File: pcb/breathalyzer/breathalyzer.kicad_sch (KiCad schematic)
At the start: 8 parts, among them U1 STM32F030K6Tx, U2 TLV73325PDBV

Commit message: voltage reference
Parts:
- added IC1: TPS3840DL25DBVR, SOT95P280X145-5N, symbol breathalyzer:TPS3840DL25DBVR
- added R1: 100k, Resistor_SMD:R_0402_1005Metric, symbol Device:R
- C1: footprint (none) -> Capacitor_SMD:C_01005_0402Metric
- C2, C3: footprint (none) -> Capacitor_SMD:C_0402_1005Metric
- C4, C5: value 100 nf -> 1 uF; footprint (none) -> Capacitor_SMD:C_0603_1608Metric
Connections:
- net +BATT: now also IC1.2 (VDD), R1.1; no longer U2.3 (EN)
- net GND: now also IC1.3 (GND)
- new net: IC1.1 (~{RESET}), R1.2, U2.3 (EN)
- no-connect marks 0 -> 2
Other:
- moved on the sheet: C4, U2

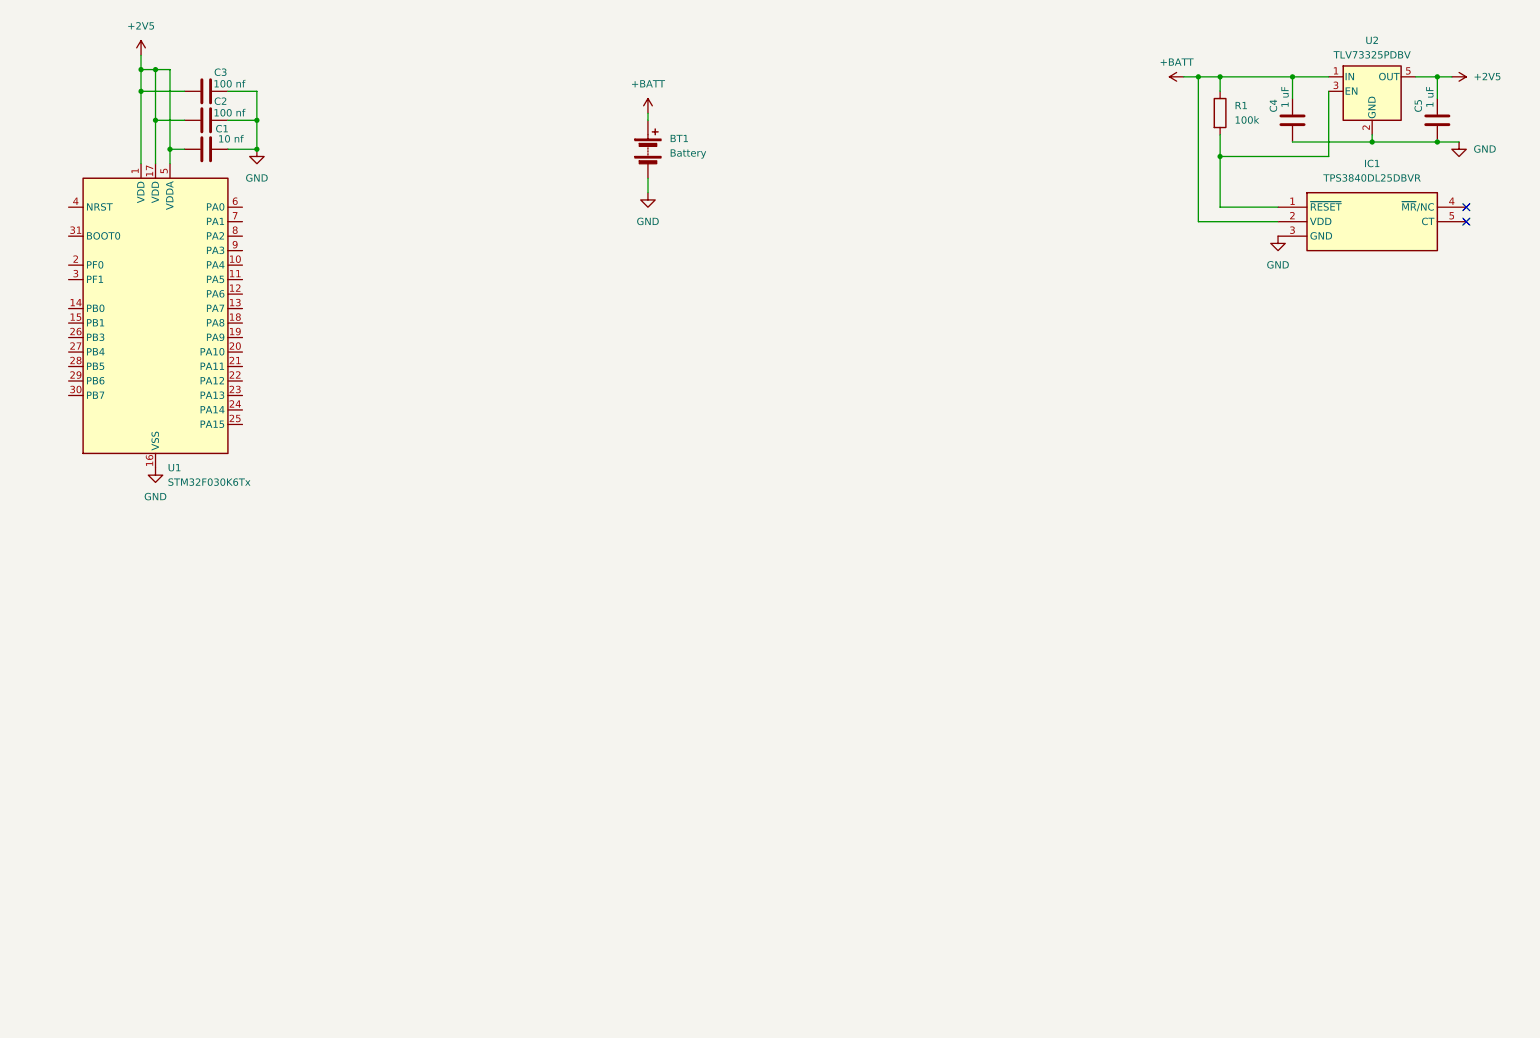
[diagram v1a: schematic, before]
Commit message: boost 3v3
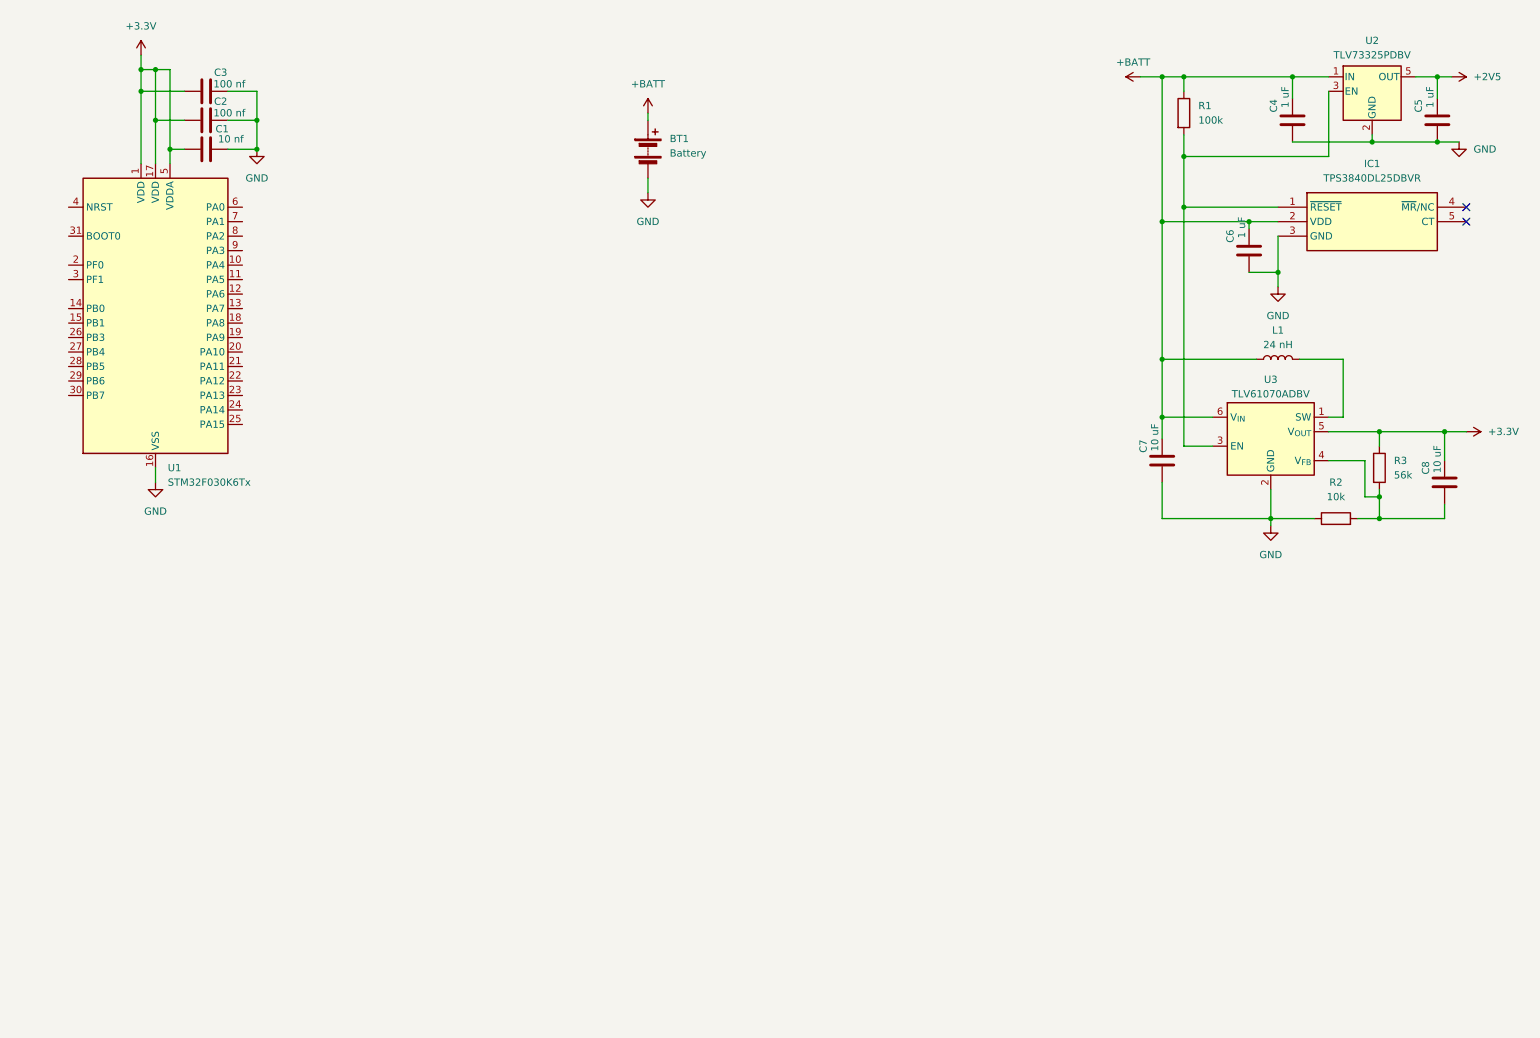
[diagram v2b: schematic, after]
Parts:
- added C6: 1 uF, Capacitor_SMD:C_0603_1608Metric, symbol Device:C
- added C7, C8: 10 uF, Capacitor_SMD:C_0805_2012Metric, symbol Device:C
- added L1: 24 nH, Inductor_SMD:L_1008_2520Metric, symbol Device:L
- added R2: 10k, Resistor_SMD:R_0603_1608Metric, symbol Device:R
- added R3: 56k, Resistor_SMD:R_0603_1608Metric, symbol Device:R
- added U3: TLV61070ADBV, Package_TO_SOT_SMD:SOT-23-6, symbol Regulator_Switching:TLV61070ADBV
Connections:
- net +2V5: no longer C1.1, C2.1, C3.1, U1.1 (VDD), U1.17 (VDD), U1.5 (VDDA)
- net +BATT: now also C6.2, C7.2, L1.1, U3.6 (V_{IN})
- net GND: now also C6.1, C7.1, R2.1, U3.2 (GND)
- net at IC1.1 (~{RESET}), R1.2, U2.3 (EN): now also U3.3 (EN)
- new net: L1.2, U3.1 (SW)
- new net: C8.1, R2.2, R3.2, U3.4 (V_{FB})
- new net +3.3V: C1.1, C2.1, C3.1, C8.2, R3.1, U1.1 (VDD), U1.17 (VDD), U1.5 (VDDA), U3.5 (V_{OUT})
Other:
- moved on the sheet: R1

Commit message: program MCU
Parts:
- added J1: 10129379-906002BLF, HDRRA6W67P0X254_1X6_1524X254X241P, symbol breathalyzer:10129379-906002BLF
- added R4: 4k7, Resistor_SMD:R_1206_3216Metric, symbol Device:R
- IC1: footprint SOT95P280X145-5N -> Package_TO_SOT_SMD:SOT-23-5_HandSoldering
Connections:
- net GND: now also J1.1, R4.2
- net USART1_TX: now reaches U1.19 (PA9)
- net USART1_TX: now also J1.3
- net USART1_RX: now reaches U1.20 (PA10)
- net USART1_RX: now also J1.2
- net BOOT0: now reaches U1.31 (BOOT0)
- net BOOT0: now also J1.4, R4.1
- net +3.3V renamed +3V3

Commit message: Serial debug
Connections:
- net SWCLK: now reaches J1.5
- net SWCLK: now also U1.24 (PA14)
- net SWDIO: now reaches J1.6
- net SWDIO: now also U1.23 (PA13)
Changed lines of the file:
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@@
+		)
+	)
+	(global_label "SWDIO"
+		(shape input)
+		(at 59.69 80.01 0)
+		(fields_autoplaced yes)
+		(effects
+			(font
+				(size 1.27 1.27)
+			)
+			(justify left)
+		)
+		(property "Intersheetrefs" "${INTERSHEET_REFS}"
+			(at 68.5414 80.01 0)
+			(effects
+				(font
+					(size 1.27 1.27)
+				)
+				(justify left)
+				(hide yes)
+			)
 		)
 	)
@@
 				)
 				(justify left)
+				(hide yes)
+			)
+		)
+	)
+	(global_label "SWCLK"
+		(shape input)
+		(at 59.69 82.55 0)
+		(fields_autoplaced yes)
+		(effects
+			(font
+				(size 1.27 1.27)
+			)
+			(justify left)
+		)
+		(property "Intersheetrefs" "${INTERSHEET_REFS}"
+			(at 68.9042 82.55 0)
+			(effects
+				(font
+					(size 1.27 1.27)
+				)
+				(justify left)
+				(hide yes)
+			)
+		)
+	)
+	(global_label "SWDIO"
+		(shape input)
+		(at 48.26 181.61 180)
+		(fields_autoplaced yes)
+		(effects
+			(font
+				(size 1.27 1.27)
+			)
+			(justify right)
+		)
+		(property "Intersheetrefs" "${INTERSHEET_REFS}"
+			(at 39.4086 181.61 0)
+			(effects
+				(font
+					(size 1.27 1.27)
+				)
+				(justify right)
 				(hide yes)
 			)
@@
 				(hide yes)
 			)
+		)
+	)
+	(global_label "SWCLK"
+		(shape input)
+		(at 48.26 179.07 180)
+		(fields_autoplaced yes)
+		(effects
+			(font
+				(size 1.27 1.27)
+			)
+			(justify right)
+		)
+		(property "Intersheetrefs" "${INTERSHEET_REFS}"
+			(at 39.0458 179.07 0)
+			(effects
+				(font
+					(size 1.27 1.27)
+				)
+				(justify right)
+				(hide yes)
+			)

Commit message: reset button
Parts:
- added SW1: PTS636SK43SMTR, breathalyzer:PTS636SM43JSMTRLFS, symbol Switch:SW_Push
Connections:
- net GND: now also SW1.2
- net NRST: now reaches U1.4 (NRST)
- net NRST: now also SW1.1
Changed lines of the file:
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@@
+	(wire
+		(pts
+			(xy 35.56 133.35) (xy 38.1 133.35)
+		)
+		(stroke
+			(width 0)
+			(type default)
+		)
+	)
 	(wire
 		(pts
@@
 		(pts
 			(xy 224.79 38.1) (xy 250.19 38.1)
+		)
+		(stroke
+			(width 0)
+			(type default)
+		)
+	)
+	(wire
+		(pts
+			(xy 48.26 133.35) (xy 50.8 133.35)
 		)
 		(stroke
@@
 		)
 	)
+	(global_label "NRST"
+		(shape input)
+		(at 29.21 46.99 180)
+		(fields_autoplaced yes)
+		(effects
+			(font
+				(size 1.27 1.27)
+			)
+			(justify right)
+		)
+		(property "Intersheetrefs" "${INTERSHEET_REFS}"
+			(at 21.4472 46.99 0)
+			(effects
+				(font
+					(size 1.27 1.27)
+				)
+				(justify right)
+				(hide yes)
+			)
+		)
+	)
 	(global_label "SWDIO"
 		(shape input)
@@
 		(property "Intersheetrefs" "${INTERSHEET_REFS}"
 			(at 21.3867 176.53 0)
+			(effects
+				(font
+					(size 1.27 1.27)
+				)
+				(justify right)
+				(hide yes)
+			)
+		)
+	)
+	(global_label "NRST"
+		(shape input)
+		(at 35.56 133.35 180)
+		(fields_autoplaced yes)
+		(effects
+			(font
+				(size 1.27 1.27)
+			)
+			(justify right)
+		)
+		(property "Intersheetrefs" "${INTERSHEET_REFS}"
+			(at 27.7972 133.35 0)
 			(effects
 				(font
@@
 					(unit 1)
 				)
+			)
+		)
+	)
+	(symbol
+		(lib_id "Switch:SW_Push")
+		(at 43.18 133.35 0)
+		(unit 1)
+		(exclude_from_sim no)
+		(in_bom yes)
+		(on_board yes)
+		(dnp no)
+		(fields_autoplaced yes)
+		(property "Reference" "SW1"
+			(at 43.18 125.73 0)
+			(effects
+				(font
+					(size 1.27 1.27)
+				)
+			)
+		)
+		(property "Value" "PTS636SK43SMTR"
+			(at 43.18 128.27 0)
+			(effects
+				(font
+					(size 1.27 1.27)
+				)
+			)
+		)
+		(property "Footprint" "breathalyzer:PTS636SM43JSMTRLFS"
+			(at 43.18 128.27 0)
+			(effects
+				(font
+					(size 1.27 1.27)
+				)
+				(hide yes)
+			)
+		)
+		(property "Datasheet" "https://hu.mouser.com/ProductDetail/CK/PTS636SK43SMTR-LFS?qs=jcD%2FCkGBYePd2dW0Qz%252BKmg%3D%3D"
+			(at 43.18 128.27 0)
+			(effects
+				(font
+					(size 1.27 1.27)
+				)
+				(hide yes)
+			)
+		)
+		(property "Description" "Push button switch, generic, two pins"
+			(at 43.18 133.35 0)
+			(effects
+				(font
+					(size 1.27 1.27)
+				)
+				(hide yes)
+			)
+		)
+		(pin "2"
+		)
+		(pin "1"
+		)
+		(instances
+			(project ""
+				(path "/e92d6a20-f7e6-42bc-b7eb-52ddd833ed75"
+					(reference "SW1")
+					(unit 1)
+				)
+			)
+		)
+	)
+	(symbol
+		(lib_id "power:GND")
+		(at 50.8 133.35 90)
+		(unit 1)
+		(exclude_from_sim no)
+		(in_bom yes)
+		(on_board yes)
+		(dnp no)
+		(property "Reference" "#PWR013"
+			(at 57.15 133.35 0)
+			(effects
+				(font
+					(size 1.27 1.27)
+				)
+				(hide yes)
+			)
+		)
+		(property "Value" "GND"
+			(at 55.88 133.35 0)
+			(effects
+				(font
+					(size 1.27 1.27)
+				)
+			)
+		)
+		(property "Footprint" ""
+			(at 50.8 133.35 0)
+			(effects
+				(font
+					(size 1.27 1.27)
+				)
+				(hide yes)
+			)
+		)
+		(property "Datasheet" ""
+			(at 50.8 133.35 0)
+			(effects
+				(font
+					(size 1.27 1.27)
+				)
+				(hide yes)
+			)
+		)
+		(property "Description" "Power symbol creates a global label with name \"GND\" , ground"
+			(at 50.8 133.35 0)
+			(effects
+				(font
+					(size 1.27 1.27)
+				)
+				(hide yes)
+			)
+		)
+		(pin "1"
+		)
+		(instances
+			(project "breathalyzer"
+				(path "/e92d6a20-f7e6-42bc-b7eb-52ddd833ed75"
+					(reference "#PWR013")
+					(unit 1)
+				)

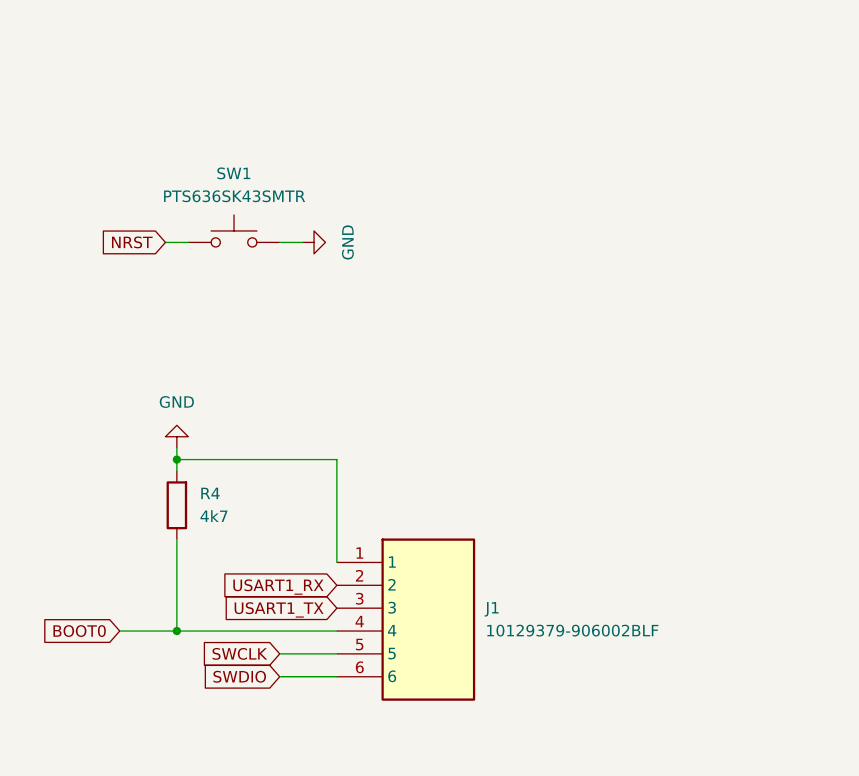
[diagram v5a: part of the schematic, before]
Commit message: change pull-down resistor for BOOT0 and bootloader mode
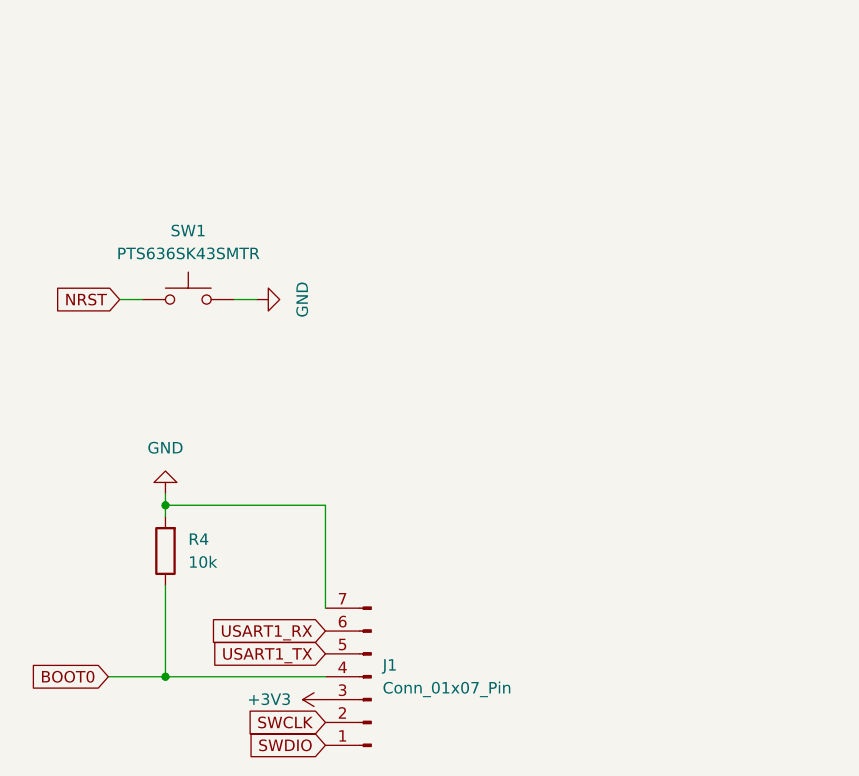
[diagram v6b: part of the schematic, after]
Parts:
- removed J1: 10129379-906002BLF, HDRRA6W67P0X254_1X6_1524X254X241P, symbol breathalyzer:10129379-906002BLF
- added J1: Conn_01x07_Pin, breathalyzer:HDRRA7W66P0X254_1X7_1778X229X274P, symbol Connector:Conn_01x07_Pin
- R4: value 4k7 -> 10k; footprint Resistor_SMD:R_1206_3216Metric -> Resistor_SMD:R_0603_1608Metric
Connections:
- net +3V3: now also J1.3 (Pin_3)
- net BOOT0: now also J1.4 (Pin_4)
- net GND: now also J1.7 (Pin_7)
- net SWCLK: now also J1.2 (Pin_2)
- net SWDIO: now also J1.1 (Pin_1)
- net USART1_RX: now also J1.6 (Pin_6)
- net USART1_TX: now also J1.5 (Pin_5)
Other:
- moved on the sheet: SW1

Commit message: wakeup button
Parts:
- added R5: 10k, Resistor_SMD:R_0603_1608Metric, symbol Device:R
- added SW2: 430162085826, breathalyzer:430162085826, symbol Switch:SW_Push
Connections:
- net +3V3: now also SW2.2
- net GND: now also R5.2
- net WKUP: now reaches U1.6 (PA0)
- net WKUP: now also R5.1, SW2.1
- no-connect marks 2 -> 4
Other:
- moved on the sheet: SW1

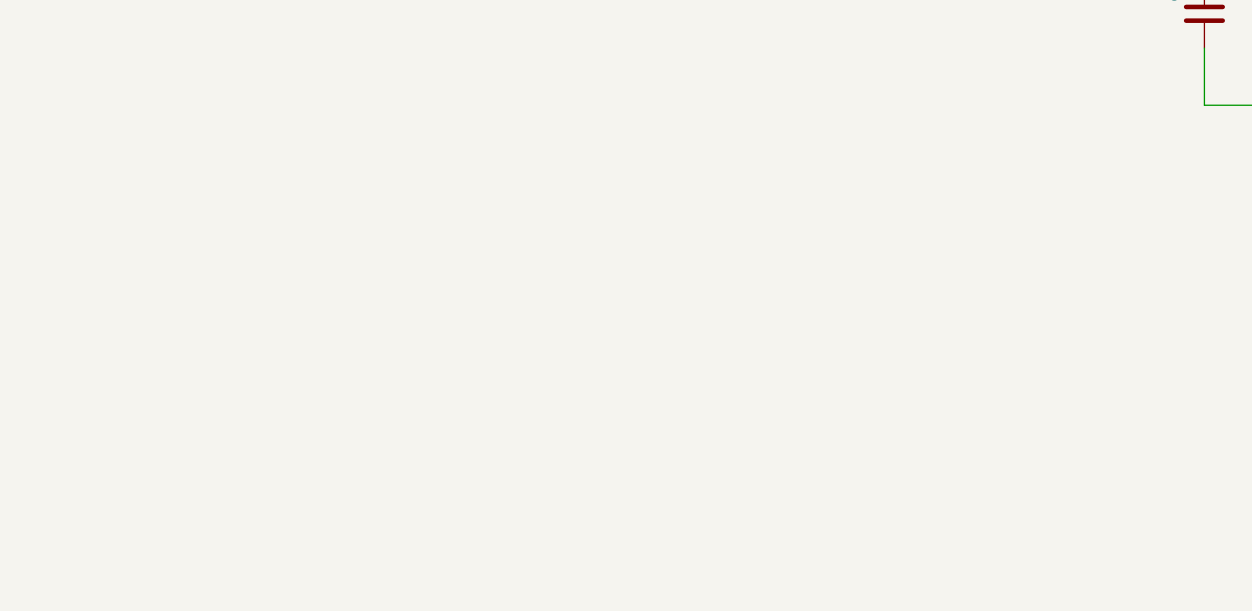
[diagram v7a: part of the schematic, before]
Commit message: display parts chosen
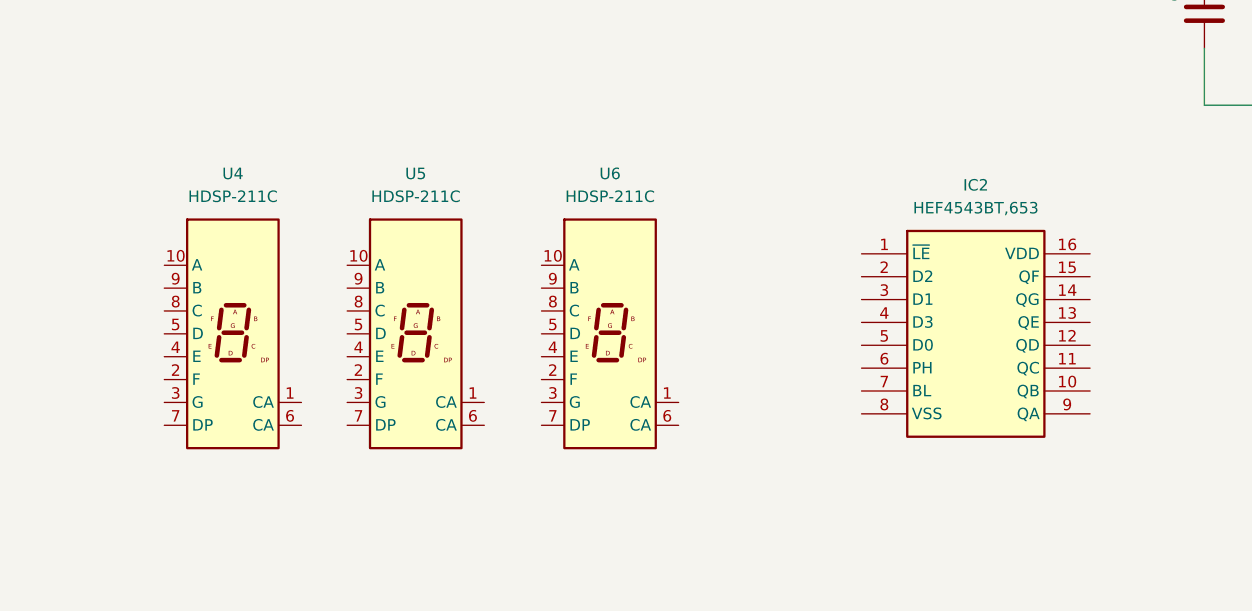
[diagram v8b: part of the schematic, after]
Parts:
- added IC2: HEF4543BT,653, breathalyzer:HEF4543BT653, symbol breathalyzer:HEF4543BT,653
- added U4, U5, U6: HDSP-211C, breathalyzer:LDSA3502RDSUG, symbol Display_Character:HDSP-7401
